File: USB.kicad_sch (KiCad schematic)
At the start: 25 parts, among them J3 USB_C_Receptacle_USB2.0, U2 TPD4E05U06QDQARQ1, U3 MCP1825ST-3302E/DB

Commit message: Improve layout
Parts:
- removed D6: D_Schottky, Diode_SMD:D_SOD-323_HandSoldering, symbol Device:D_Schottky
- removed U2: TPD4E05U06QDQARQ1, Package_SON:USON-10_2.5x1.0mm_P0.5mm, symbol Tiny_Scarab:TPD4E05U06QDQARQ1
- added C26: 100n, Capacitor_SMD:C_0402_1005Metric_Pad0.74x0.62mm_HandSolder, symbol Device:C
- added D6: SD103AWS, Tiny_Scarab:D_SOD-323, symbol Tiny_Scarab:SD103AWS
- added D8, D9: CDSOD323-T05LC, Tiny_Scarab:SOD2513X114N, symbol Tiny_Scarab:CDSOD323-T05LC
- D1, D2: footprint Diode_SMD:D_SMA -> Tiny_Scarab:D_SMA
- renumbered C7 to C10, C1 to C16, C1 to C17, C1 to C24, C10 to C6, C6 to C7, D1 to D3, R4 to R1, R5 to R2, R6 to R3
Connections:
- net +3V3: now also D6.2 (A)
- net +5V: now also C26.1, D6.1 (K)
- net GND: now also C26.2, D8.2, D9.2
- net USB_N: now also D8.1
- net USB_P: now also D9.1
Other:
- note added: "The CDSOD323-T05LC protects the USB data signals against voltage transients."
- note removed: "The TPD4E05U06QDQARQ1 protects the USB data signals against voltage transients."

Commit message: Improve layout
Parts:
- added C6, C7: 100n, Capacitor_SMD:C_0402_1005Metric_Pad0.74x0.62mm_HandSolder, symbol Device:C
- C1: renamed from C16; GPN GPC0402104-16 -> (none); MPN (none) -> GPC0402104-16
- C10: renamed from C6; GPN GPC0402106-6.3 -> (none); MPN (none) -> GPC0402106-6.3
- C11: renamed from C7; GPN GPC0402105-16 -> (none); MPN (none) -> GPC0402105-16
- C12: renamed from C4; GPN GPC0402105-16 -> (none); MPN (none) -> GPC0402105-16
- C13: renamed from C8; GPN GPC0402104-25 -> (none); MPN (none) -> GPC0402104-25
- C14: renamed from C24; GPN GPC0402104-16 -> (none); MPN (none) -> GPC0402104-16
- C15: renamed from C9; GPN GPC0402104-25 -> (none); MPN (none) -> GPC0402104-25
- C16: renamed from C10; GPN GPC0402105-16 -> (none); MPN (none) -> GPC0402105-16
- C17: renamed from C11; GPN GPC0402106-6.3 -> (none); MPN (none) -> GPC0402106-6.3
- C2: renamed from C17; GPN GPC0402104-16 -> (none); MPN (none) -> GPC0402104-16
- C3: renamed from C26; GPN GPC0402104-16 -> (none); MPN (none) -> GPC0402104-16
- C4: renamed from C1; GPN GPC0402104-16 -> (none); MPN (none) -> GPC0402104-16
- C5: renamed from C2; GPN GPC0402104-16 -> (none); MPN (none) -> GPC0402104-16
- C8: renamed from C5; GPN GPC0402104-25 -> (none); MPN (none) -> GPC0402104-25
- C9: renamed from C3; GPN GPC0402105-16 -> (none); MPN (none) -> GPC0402105-16
- R1, R2: GPN GPR04025K1 -> (none); MPN (none) -> GPR04025K1
- R3: value 470 -> 200; GPN GPR0402470R -> (none); MPN (none) -> GPR0402200R
- U1: renamed from U3; footprint Package_TO_SOT_SMD:SOT-223-3_TabPin2 -> Tiny_Scarab:SOT-223-3_TabPin2; Distributor DigiKey -> (none); Supplier (none) -> DigiKey
- renumbered D8 to D3, D9 to D4, D6 to D5, J3 to J1, D3 to LED1
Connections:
- net +5V: now also C6.1, C7.1
- net GND: now also C6.2, C7.2
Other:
- note added: "10mA 3V GREEN"
- note removed: "5mA 2V7 GREEN"
- moved on the sheet: C1, C10, C11, C12, C13, C14, C2, C3, C9, D5

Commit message: Update layout
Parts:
- D1: value SMAJ5.0A -> ~
- D2: value SMAZ5V6-TP -> ~
- D3, D4: value CDSOD323-T05LC -> ~
- D5: value SD103AWS -> ~
- F1: value SF-1206F100-2 -> ~
- LED1: value LED -> ~
- U1: value MCP1825ST-3302E/DB -> ~
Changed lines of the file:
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@@
       (effects (font (size 1.27 1.27)) (justify left))
     )
-    (property "Value" "LED" (at 195.58 41.91 0)
+    (property "Value" "~" (at 195.58 41.91 0)
       (effects (font (size 1.27 1.27)) (justify right) hide)
     )
@@
       (effects (font (size 1.27 1.27)))
     )
-    (property "Value" "SF-1206F100-2" (at 55.88 44.45 0)
+    (property "Value" "~" (at 55.88 44.45 0)
       (effects (font (size 1.27 1.27)) hide)
     )
@@
       (effects (font (size 1.27 1.27)))
     )
-    (property "Value" "SD103AWS" (at 119.0625 69.85 0)
+    (property "Value" "~" (at 119.0625 69.85 0)
       (effects (font (size 1.27 1.27)) hide)
     )
@@
       (effects (font (size 1.27 1.27)) (justify right))
     )
-    (property "Value" "CDSOD323-T05LC" (at 130.81 55.88 0)
+    (property "Value" "~" (at 130.81 55.88 0)
       (effects (font (size 0.5 0.5)) (justify left) hide)
     )
@@
       (effects (font (size 1.27 1.27)) (justify right))
     )
-    (property "Value" "SMAJ5.0A" (at 85.09 54.61 90)
-      (effects (font (size 1.27 1.27)) (justify right))
+    (property "Value" "~" (at 85.09 54.61 90)
+      (effects (font (size 1.27 1.27)) (justify right) hide)
     )
     (property "Footprint" "Tiny_Scarab:D_SMA" (at 102.87 52.07 0)
@@
       (effects (font (size 1.27 1.27)) hide)
     )
-    (property "MPN" "SMAJ5.0A" (at 90.17 52.07 0)
-      (effects (font (size 1.27 1.27)) hide)
+    (property "MPN" "SMAJ5.0A" (at 80.01 54.61 90)
+      (effects (font (size 1.27 1.27)))
     )
     (property "Supplier" "DigiKey" (at 92.71 52.07 0)
@@
       (effects (font (size 1.27 1.27)) (justify left))
     )
-    (property "Value" "SMAZ5V6-TP" (at 90.17 54.61 90)
-      (effects (font (size 1.27 1.27)) (justify left))
+    (property "Value" "~" (at 90.17 54.61 90)
+      (effects (font (size 1.27 1.27)) (justify left) hide)
     )
     (property "Footprint" "Tiny_Scarab:D_SMA" (at 96.52 52.07 0)
@@
       (effects (font (size 1.27 1.27)) hide)
     )
-    (property "MPN" "SMAZ5V6-TP" (at 104.14 52.07 0)
-      (effects (font (size 1.27 1.27)) hide)
+    (property "MPN" "SMAZ5V6-TP" (at 96.52 54.61 90)
+      (effects (font (size 1.27 1.27)))
     )
     (property "Supplier" "DigiKey" (at 101.6 52.07 0)
@@
       (effects (font (size 1.27 1.27)) (justify left))
     )
-    (property "Value" "CDSOD323-T05LC" (at 135.89 55.88 0)
+    (property "Value" "~" (at 135.89 55.88 0)
       (effects (font (size 0.5 0.5)) (justify left) hide)
     )
@@
   )
   (symbol (lib_id "Tiny_Scarab:MCP1825ST-3302E/DB") (at 119.38 85.09 0) (unit 1)
-    (in_bom yes) (on_board yes) (dnp no) (fields_autoplaced)
+    (in_bom yes) (on_board yes) (dnp no)
     (property "Reference" "U1" (at 119.38 78.74 0)
       (effects (font (size 1.27 1.27)))
     )
-    (property "Value" "MCP1825ST-3302E/DB" (at 119.38 81.28 0)
-      (effects (font (size 1.27 1.27)))
+    (property "Value" "~" (at 119.38 81.28 0)
+      (effects (font (size 1.27 1.27)) hide)
     )
     (property "Footprint" "Tiny_Scarab:SOT-223-3_TabPin2" (at 119.38 64.77 0)
@@
       (effects (font (size 1.27 1.27)) hide)
     )
-    (property "MPN" "MCP1825ST-3302E/DB" (at 119.38 69.85 0)
-      (effects (font (size 1.27 1.27)) hide)
+    (property "MPN" "MCP1825ST-3302E/DB" (at 120.65 81.28 0)
+      (effects (font (size 1.27 1.27)))
     )
     (property "Supplier" "DigiKey" (at 119.38 72.39 0)

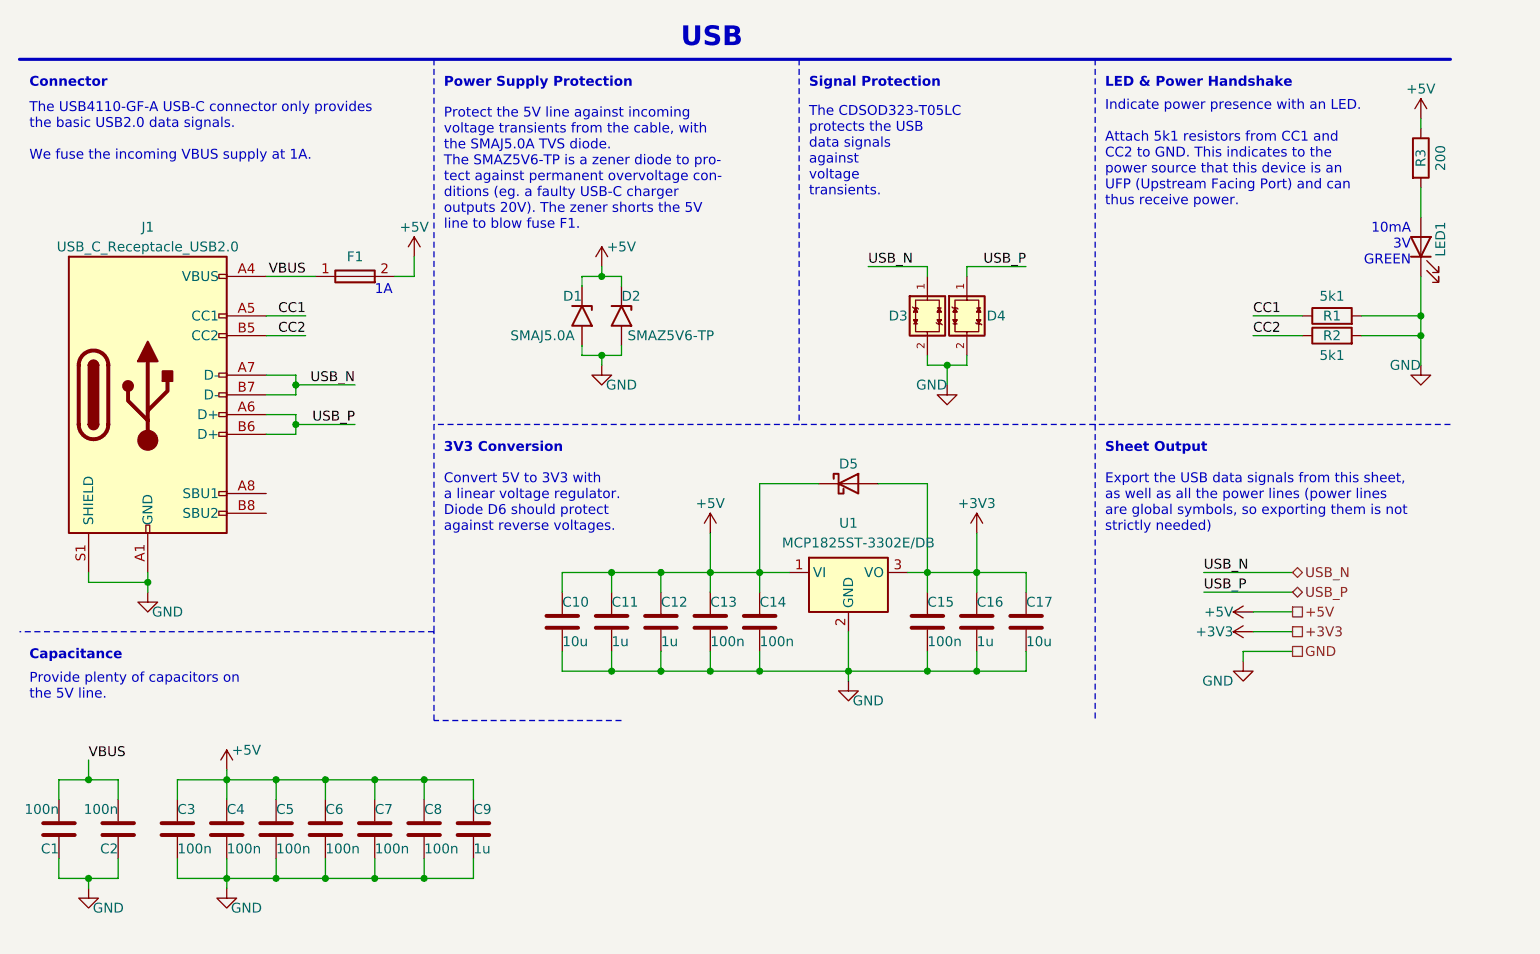
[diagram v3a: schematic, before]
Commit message: Prepare PCB for JLCPCB production
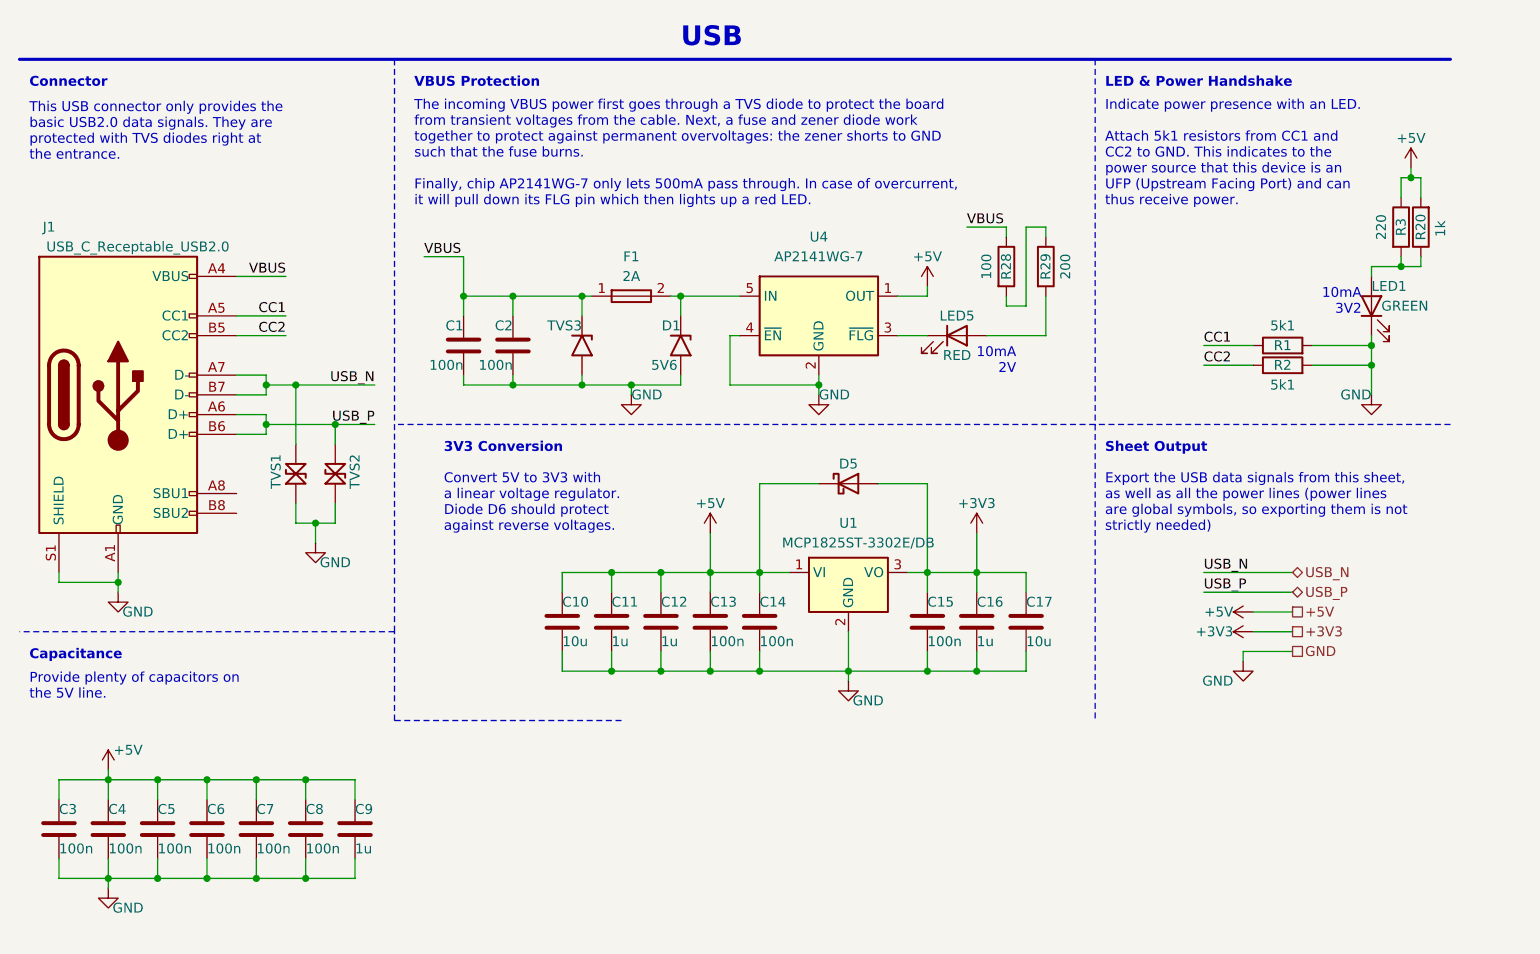
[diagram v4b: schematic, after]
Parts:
- removed D1: ~, Tiny_Scarab:D_SMA, symbol Tiny_Scarab:SMAJ5.0A
- removed D2: ~, Tiny_Scarab:D_SMA, symbol Tiny_Scarab:SMAZ5V6-TP
- removed F1: ~, Fuse:Fuse_1206_3216Metric_Pad1.42x1.75mm_HandSolder, symbol Tiny_Scarab:SF-1206F100-2
- removed J1: USB_C_Receptacle_USB2.0, Tiny_Scarab:USB_C_Receptacle_GCT_USB4110, symbol Tiny_Scarab:USB_C_Receptacle_USB2.0
- removed LED1: ~, LED_SMD:LED_0603_1608Metric_Pad1.05x0.95mm_HandSolder, symbol Device:LED
- added D1: 5V6, Tiny_Scarab:D_SMA_1SMA4734A, symbol Tiny_Scarab:D_ZENER_1SMA4734A
- added F1: 2A, Tiny_Scarab:Fuse_MFU0603FF02000P500, symbol Tiny_Scarab:FUSE_MFU0603FF02000P500
- added J1: USB_C_Receptable_USB2.0, Tiny_Scarab:USB_C_Receptable_USB-TYPE-C-018, symbol Tiny_Scarab:USB_C_Receptable_USB2.0
- added LED1: GREEN, Tiny_Scarab:LED_0603_CSL0902ET, symbol Tiny_Scarab:LED_GREEN_CSL0902ET
- added LED5: RED, Tiny_Scarab:LED_0603_CSL0902UT, symbol Tiny_Scarab:LED_RED_CSL0902UT
- added R20: 1k, Resistor_SMD:R_0402_1005Metric_Pad0.72x0.64mm_HandSolder, symbol Device:R
- added R28: 100, Resistor_SMD:R_0402_1005Metric_Pad0.72x0.64mm_HandSolder, symbol Device:R
- added R29: 200, Resistor_SMD:R_0402_1005Metric_Pad0.72x0.64mm_HandSolder, symbol Device:R
- added TVS3: 5V, Tiny_Scarab:D_SMA_SMAJ5.0A, symbol Tiny_Scarab:TVS_SMAJ5.0A
- added U4: AP2141WG-7, Tiny_Scarab:SOT-23-5, symbol Tiny_Scarab:AP2141WG-7
- C1, C2: Comment (none) -> 50V 100nF X7R ±10% 0402 Multilayer Ceramic Capacitors MLCC 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; JLCPCB Part # (none) -> C307331; MPN GPC0402104-16 -> CL05B104KB54PNC; Manufacturer (none) -> Samsung electro-mechanics
- C10: JLCPCB Part # (none) -> C15525; MPN GPC0402106-6.3 -> CL05A106MQ5NUNC; Manufacturer (none) -> Samsung Electro-Mechanics
- C11, C12, C16, C9: JLCPCB Part # (none) -> C52923; MPN GPC0402105-16 -> CL05A105KA5NQNC; Manufacturer (none) -> Samsung electro-mechanics
- C13, C15, C8: JLCPCB Part # (none) -> C1525; MPN GPC0402104-25 -> CL05B104KO5NNNC; Manufacturer (none) -> Samsung electro-mechanics
- C14, C3, C4, C5, C6, C7: JLCPCB Part # (none) -> C1525; MPN GPC0402104-16 -> CL05B104KO5NNNC; Manufacturer (none) -> Samsung electro-mechanics
- C17: JLCPCB Part # (none) -> C15525; MPN GPC0402106-6.3 -> CL05A106MQ5NUNC; Manufacturer (none) -> Samsung electro-mechanics
- D5: JLCPCB Part # (none) -> C397613
- R1, R2: JLCPCB Part # (none) -> C25905; MPN GPR04025K1 -> 0402WGF5101TCE; Manufacturer (none) -> UNI-ROYAL(Uniroyal Elec)
- R3: value 200 -> 220; JLCPCB Part # (none) -> C25091; MPN GPR0402200R -> 0402WGF2200TCE; Manufacturer (none) -> UNI-ROYAL(Uniroyal Elec)
- TVS1: renamed from D3; value ~ -> 5V; footprint Tiny_Scarab:SOD2513X114N -> Tiny_Scarab:D_SOD-323_CDSOD323-T05LC; DigiKey (none) -> CDSOD323-T05LCTR-ND; JLCPCB Part # (none) -> C840637
- TVS2: renamed from D4; value ~ -> 5V; footprint Tiny_Scarab:SOD2513X114N -> Tiny_Scarab:D_SOD-323_CDSOD323-T05LC; DigiKey (none) -> CDSOD323-T05LCTR-ND; JLCPCB Part # (none) -> C840637
- U1: JLCPCB Part # (none) -> C145411
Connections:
- net +5V: now also R20.2, U4.1 (OUT)
- net CC1: now also J1.A5 (CC1)
- net CC2: now also J1.B5 (CC2)
- net GND: now also D1.2 (A2), J1.A1 (GND), J1.A12 (GND), J1.B1 (GND), J1.B12 (GND), J1.S1 (SHIELD), LED1.1 (K), TVS3.2 (A2), U4.2 (GND), U4.4 (~{EN})
- net USB_N: now also J1.A7 (D-), J1.B7 (D-)
- net USB_P: now also J1.A6 (D+), J1.B6 (D+)
- net VBUS: now also F1.1, J1.A4 (VBUS), J1.A9 (VBUS), J1.B4 (VBUS), J1.B9 (VBUS), R28.1, TVS3.1 (A1)
- net at R3.2: now also LED1.2 (A), R20.1
- new net: R28.2, R29.1
- new net: LED5.2 (A), R29.2
- new net: D1.1 (A1), F1.2, U4.5 (IN)
- new net: LED5.1 (K), U4.3 (~{FLG})
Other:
- note added: "10mA 2V"
- note added: "10mA 3V2"
- note added: "The incoming VBUS power first goes through a TVS diode to protect the board from transient voltages from the cable. Next, a fuse and zener diode work together to protect against permanent overvoltages: the zener shorts to GND such that the fuse burns. Finally, chip AP2141WG-7 only lets 500mA pass through. In case of overcurrent, it will pull down its FLG pin which then lights up a red LED."
- note added: "This USB connector only provides the basic USB2.0 data signals. They are protected with TVS diodes right at the entrance."
- note added: "VBUS Protection"
- note removed: "10mA 3V GREEN"
- note removed: "1A"
- note removed: "Power Supply Protection"
- note removed: "Protect the 5V line against incoming voltage transients from the cable, with the SMAJ5.0A TVS diode. The SMAZ5V6-TP is a zener diode to pro- tect against permanent overvoltage con- ditions (eg. a faulty USB-C charger outputs 20V). The zener shorts the 5V line to blow fuse F1."
- note removed: "Signal Protection"
- note removed: "The CDSOD323-T05LC protects the USB data signals against voltage transients."
- note removed: "The USB4110-GF-A USB-C connector only provides the basic USB2.0 data signals. We fuse the incoming VBUS supply at 1A."
- moved on the sheet: C1, C3, C4, C5, C6, C7, C8, C9, R1, R2, R3
